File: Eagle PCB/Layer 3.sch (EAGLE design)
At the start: 88 parts, among them Q1 AO3402, Q2 AO3402, X1 SM06B-SRSS-TB, Y1 8MHz

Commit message: Hello
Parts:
- removed 3RD_LAYER: (no value), SparkFun-Connectors:CONN_05LOCK
- removed ESC_IN, SERVO_IO: (no value), SparkFun-Connectors:CONN_03LOCK
- removed ESC_OUT: XT30PB-F, JH:XT30PB-F
- removed Q1, Q2: AO3402, SparkFun-DiscreteSemi:MOSFET-NCH-AO3404A
- removed R10, R11, R12, R13: 4.7k, JH:RESISTOR0603
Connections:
- removed net ESC_HV: ESC_IN.3, Q1.D, R10.2
- removed net N$4: ESC_IN.2
- removed net SERVO_HV: Q2.D, R12.2, SERVO_IO.3
- removed net V_BATT: ESC_OUT.P$V+
- net 3.3V: no longer 3RD_LAYER.2, Q1.G, Q2.G, R11.1, R13.1
- net 5V: no longer 3RD_LAYER.5, R10.1, R12.1, SERVO_IO.2
- net ESC_LV: no longer 3RD_LAYER.4, Q1.S, R11.2
- net GND: no longer 3RD_LAYER.1, ESC_IN.1, ESC_OUT.P$V-, SERVO_IO.1
- net SERVO_LV: no longer 3RD_LAYER.3, Q2.S, R13.2

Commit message: FUCK YOU
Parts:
- added 3RD_LAYER: (no value), SparkFun-Connectors:CONN_05LOCK
- added ESC_IN, SERVO_IO: (no value), SparkFun-Connectors:CONN_03LOCK
- added ESC_OUT: XT30PB-F, JH:XT30PB-F
- added Q1, Q2: AO3402, SparkFun-DiscreteSemi:MOSFET-NCH-AO3404A
- added R10, R11, R12, R13: 4.7k, JH:RESISTOR0603
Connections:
- new net ESC_HV: ESC_IN.3, Q1.D, R10.2
- new net N$4: ESC_IN.2
- new net SERVO_HV: Q2.D, R12.2, SERVO_IO.3
- new net V_BATT: ESC_OUT.P$V+
- net 3.3V: now also 3RD_LAYER.2, Q1.G, Q2.G, R11.1, R13.1
- net 5V: now also 3RD_LAYER.5, R10.1, R12.1, SERVO_IO.2
- net ESC_LV: now also 3RD_LAYER.4, Q1.S, R11.2
- net GND: now also 3RD_LAYER.1, ESC_IN.1, ESC_OUT.P$V-, SERVO_IO.1
- net SERVO_LV: now also 3RD_LAYER.3, Q2.S, R13.2

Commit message: Done
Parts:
- removed 3RD_LAYER: (no value), SparkFun-Connectors:CONN_05LOCK
- removed ESC_IN: (no value), SparkFun-Connectors:CONN_03LOCK
- removed ESC_OUT: XT30PB-F, JH:XT30PB-F
- added J1: (no value), Connectors:CONN_01
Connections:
- removed net N$4: ESC_IN.2
- removed net V_BATT: ESC_OUT.P$V+
- net 3.3V: no longer 3RD_LAYER.2
- net 5V: now also J1.1; no longer 3RD_LAYER.5
- net ESC_HV: no longer ESC_IN.3
- net ESC_LV: no longer 3RD_LAYER.4
- net GND: no longer 3RD_LAYER.1, ESC_IN.1, ESC_OUT.P$V-
- net SERVO_LV: no longer 3RD_LAYER.3
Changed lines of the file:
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@@
 <part name="SUPPLY7" library="SparkFun-PowerSymbols" deviceset="5V" device=""/>
 <part name="SUPPLY8" library="SparkFun-PowerSymbols" deviceset="3.3V" device=""/>
-<part name="GND41" library="SparkFun-PowerSymbols" deviceset="GND" device=""/>
 <part name="GND42" library="SparkFun-PowerSymbols" deviceset="GND" device=""/>
 <part name="SUPPLY9" library="SparkFun-PowerSymbols" deviceset="5V" device=""/>
-<part name="SUPPLY3" library="SparkFun-PowerSymbols" deviceset="V_BATT" device=""/>
-<part name="GND43" library="SparkFun-PowerSymbols" deviceset="GND" device=""/>
-<part name="GND44" library="SparkFun-PowerSymbols" deviceset="GND" device=""/>
-<part name="SUPPLY10" library="SparkFun-PowerSymbols" deviceset="3.3V" device=""/>
-<part name="ESC_IN" library="SparkFun-Connectors" library_urn="urn:adsk.eagle:library:11010760" deviceset="CONN_03" device="LOCK" package3d_urn="urn:adsk.eagle:package:11011273/2"/>
 <part name="SERVO_IO" library="SparkFun-Connectors" library_urn="urn:adsk.eagle:library:11010760" deviceset="CONN_03" device="LOCK" package3d_urn="urn:adsk.eagle:package:11011273/2"/>
-<part name="ESC_OUT" library="JH" library_urn="urn:adsk.eagle:library:6027132" deviceset="XT30" device="PB-F" package3d_urn="urn:adsk.eagle:package:15925142/7"/>
-<part name="SUPPLY11" library="SparkFun-PowerSymbols" deviceset="5V" device=""/>
-<part name="3RD_LAYER" library="SparkFun-Connectors" library_urn="urn:adsk.eagle:library:11010760" deviceset="CONN_05" device="LOCK" package3d_urn="urn:adsk.eagle:package:11011302/2"/>
+<part name="J1" library="Connectors" library_urn="urn:adsk.eagle:library:19813715" deviceset="CONN_01" device="" package3d_urn="urn:adsk.eagle:package:19813825/2"/>
+<part name="SUPPLY3" library="SparkFun-PowerSymbols" deviceset="5V" device=""/>
 </parts>
 <sheets>
@@
 <attribute name="VALUE" x="149.86" y="124.714" size="1.778" layer="96" align="bottom-center"/>
 </instance>
-<instance part="GND41" gate="1" x="99.06" y="71.12" smashed="yes">
-<attribute name="VALUE" x="99.06" y="70.866" size="1.778" layer="96" align="top-center"/>
-</instance>
 <instance part="GND42" gate="1" x="167.64" y="71.12" smashed="yes">
 <attribute name="VALUE" x="167.64" y="70.866" size="1.778" layer="96" align="top-center"/>
@@
 <instance part="SUPPLY9" gate="G$1" x="177.8" y="88.9" smashed="yes">
 <attribute name="VALUE" x="177.8" y="91.694" size="1.778" layer="96" align="bottom-center"/>
-</instance>
-<instance part="SUPPLY3" gate="G$1" x="60.96" y="91.44" smashed="yes">
-<attribute name="VALUE" x="60.96" y="94.234" size="1.778" layer="96" align="bottom-center"/>
-</instance>
-<instance part="GND43" gate="1" x="60.96" y="73.66" smashed="yes">
-<attribute name="VALUE" x="60.96" y="73.406" size="1.778" layer="96" align="top-center"/>
-</instance>
-<instance part="GND44" gate="1" x="121.92" y="38.1" smashed="yes">
-<attribute name="VALUE" x="121.92" y="37.846" size="1.778" layer="96" align="top-center"/>
-</instance>
-<instance part="SUPPLY10" gate="G$1" x="129.54" y="53.34" smashed="yes">
-<attribute name="VALUE" x="129.54" y="56.134" size="1.778" layer="96" align="bottom-center"/>
-</instance>
-<instance part="ESC_IN" gate="J$1" x="81.28" y="81.28" smashed="yes">
-<attribute name="VALUE" x="78.74" y="73.914" size="1.778" layer="96" font="vector"/>
-<attribute name="NAME" x="78.74" y="86.868" size="1.778" layer="95" font="vector"/>
 </instance>
 <instance part="SERVO_IO" gate="J$1" x="149.86" y="81.28" smashed="yes">
@@
 <attribute name="NAME" x="147.32" y="86.868" size="1.778" layer="95" font="vector"/>
 </instance>
-<instance part="ESC_OUT" gate="G$1" x="60.96" y="83.82" smashed="yes">
-<attribute name="NAME" x="57.658" y="78.74" size="1.778" layer="95" font="vector" rot="R90"/>
-<attribute name="VALUE" x="66.04" y="78.74" size="1.778" layer="95" font="vector" rot="R90"/>
-</instance>
-<instance part="SUPPLY11" gate="G$1" x="114.3" y="58.42" smashed="yes">
-<attribute name="VALUE" x="114.3" y="61.214" size="1.778" layer="96" align="bottom-center"/>
-</instance>
-<instance part="3RD_LAYER" gate="G$1" x="101.6" y="50.8" smashed="yes">
-<attribute name="VALUE" x="99.06" y="40.894" size="1.778" layer="96" font="vector"/>
-<attribute name="NAME" x="99.06" y="58.928" size="1.778" layer="95" font="vector"/>
+<instance part="J1" gate="G$1" x="93.98" y="88.9" smashed="yes">
+<attribute name="VALUE" x="91.44" y="84.074" size="1.778" layer="96" font="vector"/>
+<attribute name="NAME" x="91.44" y="91.948" size="1.778" layer="95" font="vector"/>
+</instance>
+<instance part="SUPPLY3" gate="G$1" x="101.6" y="91.44" smashed="yes">
+<attribute name="VALUE" x="101.6" y="94.234" size="1.778" layer="96" align="bottom-center"/>
 </instance>
 </instances>
@@
 <label x="83.82" y="129.54" size="1.778" layer="95"/>
 </segment>
-<segment>
-<wire x1="88.9" y1="83.82" x2="101.6" y2="83.82" width="0.1524" layer="91"/>
-<label x="91.44" y="83.82" size="1.778" layer="95"/>
-<pinref part="ESC_IN" gate="J$1" pin="3"/>
-</segment>
 </net>
 <net name="5V" class="0">
@@
 </segment>
 <segment>
-<wire x1="109.22" y1="55.88" x2="114.3" y2="55.88" width="0.1524" layer="91"/>
-<wire x1="114.3" y1="55.88" x2="114.3" y2="58.42" width="0.1524" layer="91"/>
-<pinref part="SUPPLY11" gate="G$1" pin="5V"/>
-<pinref part="3RD_LAYER" gate="G$1" pin="5"/>
+<pinref part="SUPPLY3" gate="G$1" pin="5V"/>
+<pinref part="J1" gate="G$1" pin="1"/>
+<wire x1="101.6" y1="91.44" x2="101.6" y2="88.9" width="0.1524" layer="91"/>
 </segment>
 </net>
@@
 <junction x="149.86" y="119.38"/>
 </segment>
-<segment>
-<wire x1="109.22" y1="48.26" x2="129.54" y2="48.26" width="0.1524" layer="91"/>
-<wire x1="129.54" y1="48.26" x2="129.54" y2="53.34" width="0.1524" layer="91"/>
-<pinref part="SUPPLY10" gate="G$1" pin="3.3V"/>
-<pinref part="3RD_LAYER" gate="G$1" pin="2"/>
-</segment>
 </net>
 <net name="ESC_LV" class="0">
@@
 <label x="83.82" y="114.3" size="1.778" layer="95"/>
 </segment>
-<segment>
-<wire x1="109.22" y1="53.34" x2="124.46" y2="53.34" width="0.1524" layer="91"/>
-<label x="111.76" y="53.34" size="1.778" layer="95"/>
-<pinref part="3RD_LAYER" gate="G$1" pin="4"/>
-</segment>
 </net>
 <net name="SERVO_HV" class="0">
@@
 <label x="165.1" y="114.3" size="1.778" layer="95"/>
 </segment>
-<segment>
-<wire x1="109.22" y1="50.8" x2="124.46" y2="50.8" width="0.1524" layer="91"/>
-<label x="111.76" y="50.8" size="1.778" layer="95"/>
-<pinref part="3RD_LAYER" gate="G$1" pin="3"/>
-</segment>
 </net>
 <net name="GND" class="0">
-<segment>
-<wire x1="88.9" y1="78.74" x2="99.06" y2="78.74" width="0.1524" layer="91"/>
-<wire x1="99.06" y1="78.74" x2="99.06" y2="73.66" width="0.1524" layer="91"/>
-<pinref part="GND41" gate="1" pin="GND"/>
-<pinref part="ESC_IN" gate="J$1" pin="1"/>
-</segment>
 <segment>
 <wire x1="157.48" y1="78.74" x2="167.64" y2="78.74" width="0.1524" layer="91"/>
@@
 <pinref part="SERVO_IO" gate="J$1" pin="1"/>
 </segment>
-<segment>
-<wire x1="109.22" y1="45.72" x2="121.92" y2="45.72" width="0.1524" layer="91"/>
-<wire x1="121.92" y1="45.72" x2="121.92" y2="40.64" width="0.1524" layer="91"/>
-<pinref part="GND44" gate="1" pin="GND"/>
-<pinref part="3RD_LAYER" gate="G$1" pin="1"/>
-</segment>
-<segment>
-<pinref part="GND43" gate="1" pin="GND"/>
-<pinref part="ESC_OUT" gate="G$1" pin="P$V-"/>
-</segment>
-</net>
-<net name="N$4" class="0">
-<segment>
-<wire x1="88.9" y1="81.28" x2="101.6" y2="81.28" width="0.1524" layer="91"/>
-<pinref part="ESC_IN" gate="J$1" pin="2"/>
-</segment>
-</net>
-<net name="V_BATT" class="0">
-<segment>
-<pinref part="SUPPLY3" gate="G$1" pin="V_BATT"/>
-<pinref part="ESC_OUT" gate="G$1" pin="P$V+"/>
-</segment>
-</net>
+</net>

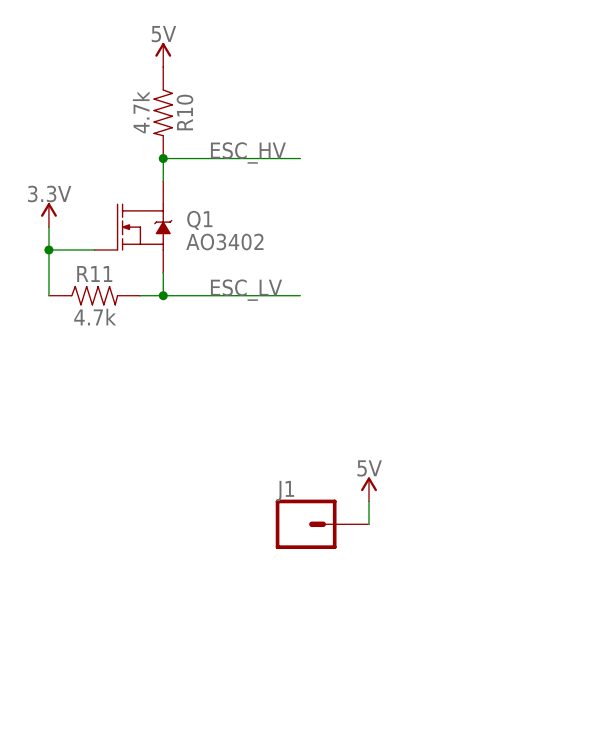
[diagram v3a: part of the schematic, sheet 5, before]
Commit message: layer 1 esc fix
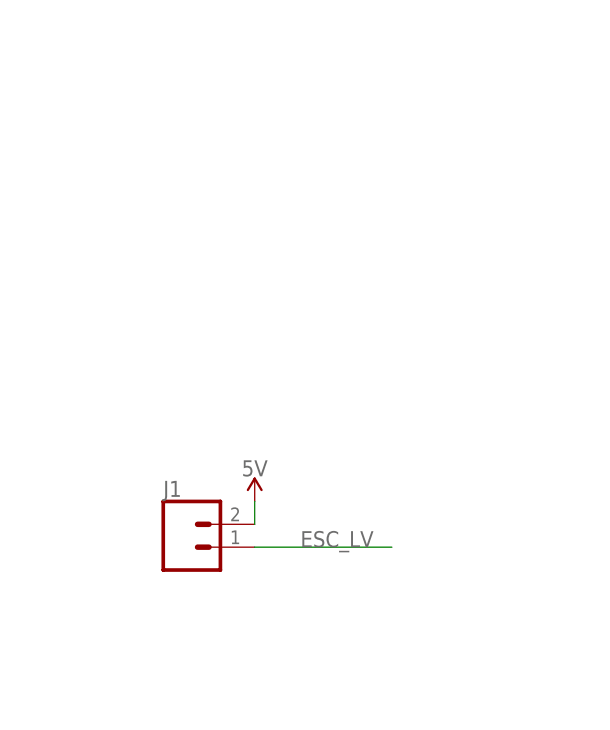
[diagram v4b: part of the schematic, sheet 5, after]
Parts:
- removed 2ND_LAYER: (no value), SparkFun-Connectors:CONN_05LOCK
- removed Q1: AO3402, SparkFun-DiscreteSemi:MOSFET-NCH-AO3404A
- removed R10, R11: 4.7k, JH:RESISTOR0603
- J1: device Connectors:CONN_01 -> Connectors:CONN_02LOCK
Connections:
- removed net ESC_HV: Q1.D, R10.2
- net 3.3V: no longer 2ND_LAYER.2, Q1.G, R11.1
- net 5V: now also J1.2; no longer 2ND_LAYER.5, J1.1, R10.1
- net ESC_LV: now also J1.1; no longer 2ND_LAYER.4, Q1.S, R11.2
- net GND: no longer 2ND_LAYER.1
- net SERVO_LV: no longer 2ND_LAYER.3
